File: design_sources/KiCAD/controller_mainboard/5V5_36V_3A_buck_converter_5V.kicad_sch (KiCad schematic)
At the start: 13 parts, among them U5 TPS5430DDA

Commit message: Continued development on the schematic. Pins wired. TODO validate.
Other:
- company: Kestech -> Mete Han Keskin
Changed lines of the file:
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@@
 		(date "2025-03-01")
 		(rev "V1.0")
-		(company "Kestech")
-		(comment 1 "MIT License. Copyright (c) 2025 Kestech Fontys")
+		(company "Mete Han Keskin")
+		(comment 1 "MIT License. Copyright (c) 2025 kestech.net")
 	)
 	(text "Vout is 4.88V specifically"

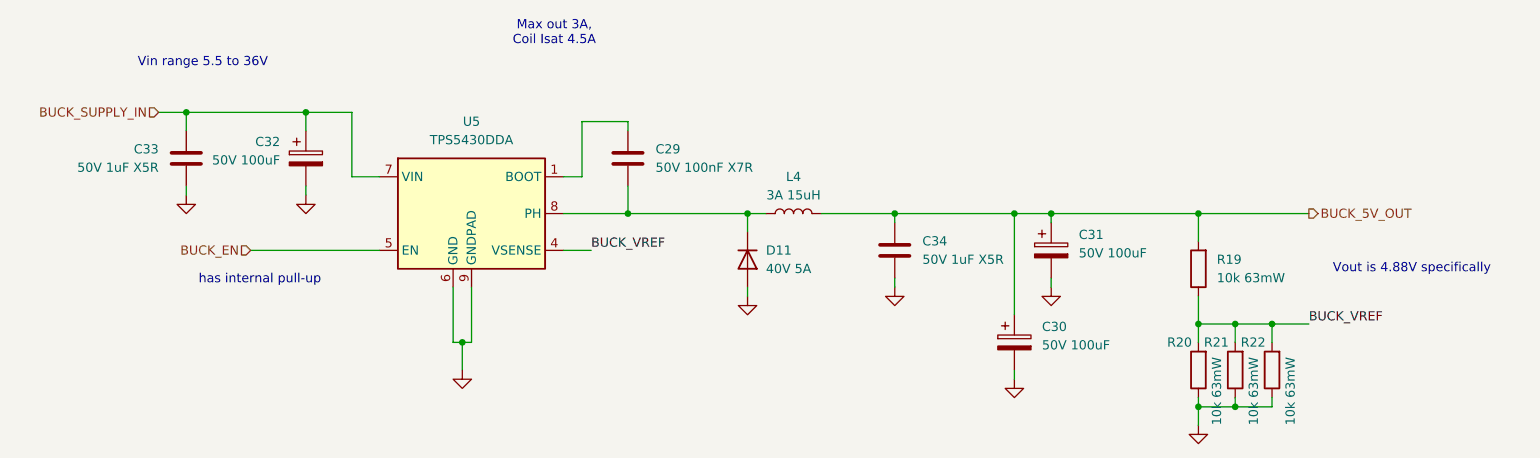
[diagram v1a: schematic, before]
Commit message: Added ESD protection ic, added footprints to all IC and loaded into pcbnew to size up the pcb size.
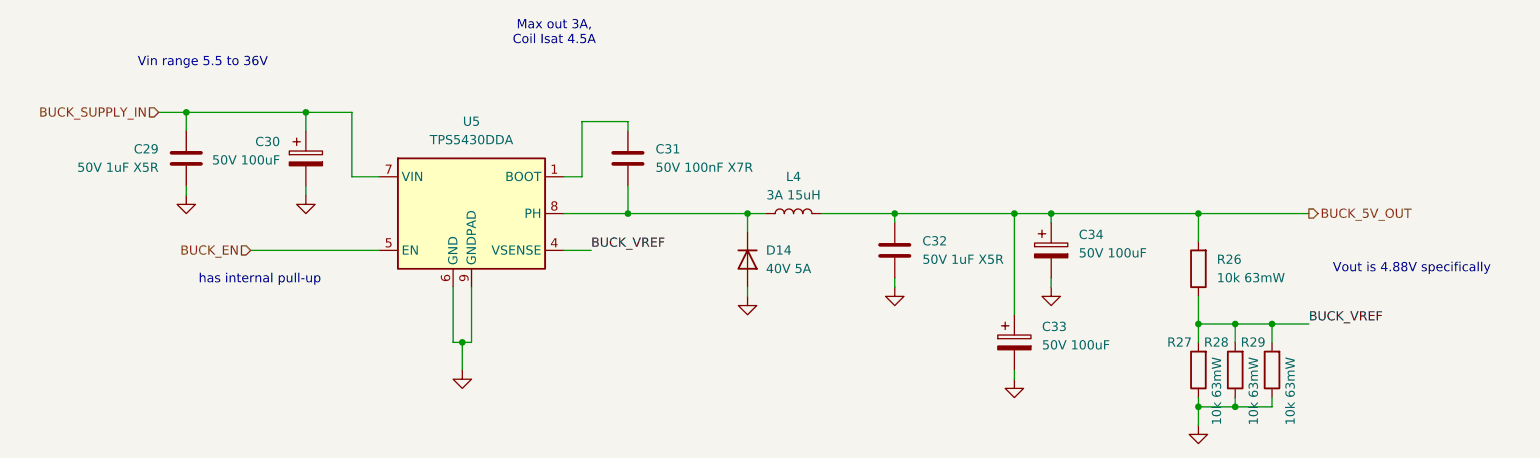
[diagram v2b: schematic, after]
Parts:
- L4: footprint (none) -> Inductor_SMD:L_APV_APH0630
- renumbered C33 to C29, C32 to C30, C29 to C31, C34 to C32, C30 to C33, C31 to C34, D11 to D14, R19 to R26, R20 to R27, R21 to R28, R22 to R29
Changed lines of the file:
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@@
 		(dnp no)
 		(fields_autoplaced yes)
-		(property "Reference" "#PWR031"
+		(property "Reference" "#PWR077"
 			(at 161.29 101.6 0)
 			(effects
@@
 			(project "controller_mainboard"
 				(path "/0fdfffec-3d24-4249-8ba9-dae7a6ccc250/f942a5b5-54c0-4fcc-a043-1f1cc07d1d6d"
-					(reference "#PWR031")
+					(reference "#PWR077")
 					(unit 1)
 				)
@@
 		(dnp no)
 		(fields_autoplaced yes)
-		(property "Reference" "#PWR033"
+		(property "Reference" "#PWR079"
 			(at 182.88 101.6 0)
 			(effects
@@
 			(project "controller_mainboard"
 				(path "/0fdfffec-3d24-4249-8ba9-dae7a6ccc250/f942a5b5-54c0-4fcc-a043-1f1cc07d1d6d"
-					(reference "#PWR033")
+					(reference "#PWR079")
 					(unit 1)
 				)
@@
 		(dnp no)
 		(fields_autoplaced yes)
-		(property "Reference" "C31"
+		(property "Reference" "C34"
 			(at 186.69 88.0109 0)
 			(effects
@@
 			(project "controller_mainboard"
 				(path "/0fdfffec-3d24-4249-8ba9-dae7a6ccc250/f942a5b5-54c0-4fcc-a043-1f1cc07d1d6d"
-					(reference "C31")
+					(reference "C34")
 					(unit 1)
 				)
@@
 		(dnp no)
 		(fields_autoplaced yes)
-		(property "Reference" "#PWR035"
+		(property "Reference" "#PWR076"
 			(at 140.97 102.87 0)
 			(effects
@@
 			(project "controller_mainboard"
 				(path "/0fdfffec-3d24-4249-8ba9-dae7a6ccc250/f942a5b5-54c0-4fcc-a043-1f1cc07d1d6d"
-					(reference "#PWR035")
+					(reference "#PWR076")
 					(unit 1)
 				)
@@
 		(dnp no)
 		(fields_autoplaced yes)
-		(property "Reference" "#PWR030"
+		(property "Reference" "#PWR074"
 			(at 80.01 88.9 0)
 			(effects
@@
 			(project "controller_mainboard"
 				(path "/0fdfffec-3d24-4249-8ba9-dae7a6ccc250/f942a5b5-54c0-4fcc-a043-1f1cc07d1d6d"
-					(reference "#PWR030")
+					(reference "#PWR074")
 					(unit 1)
 				)
@@
 		(dnp no)
 		(fields_autoplaced yes)
-		(property "Reference" "C30"
+		(property "Reference" "C33"
 			(at 181.61 100.7109 0)
 			(effects
@@
 			(project "controller_mainboard"
 				(path "/0fdfffec-3d24-4249-8ba9-dae7a6ccc250/f942a5b5-54c0-4fcc-a043-1f1cc07d1d6d"
-					(reference "C30")
+					(reference "C33")
 					(unit 1)
 				)
@@
 		(on_board yes)
 		(dnp no)
-		(property "Reference" "R21"
+		(property "Reference" "R28"
 			(at 203.962 102.87 0)
 			(effects
@@
 			(project "controller_mainboard"
 				(path "/0fdfffec-3d24-4249-8ba9-dae7a6ccc250/f942a5b5-54c0-4fcc-a043-1f1cc07d1d6d"
-					(reference "R21")
+					(reference "R28")
 					(unit 1)
 				)
@@
 		(dnp no)
 		(fields_autoplaced yes)
-		(property "Reference" "#PWR036"
+		(property "Reference" "#PWR080"
 			(at 203.2 120.65 0)
 			(effects
@@
 			(project "controller_mainboard"
 				(path "/0fdfffec-3d24-4249-8ba9-dae7a6ccc250/f942a5b5-54c0-4fcc-a043-1f1cc07d1d6d"
-					(reference "#PWR036")
+					(reference "#PWR080")
 					(unit 1)
 				)
@@
 		(dnp no)
 		(fields_autoplaced yes)
-		(property "Reference" "C29"
+		(property "Reference" "C31"
 			(at 128.27 76.1999 0)
 			(effects
@@
 			(project "controller_mainboard"
 				(path "/0fdfffec-3d24-4249-8ba9-dae7a6ccc250/f942a5b5-54c0-4fcc-a043-1f1cc07d1d6d"
-					(reference "C29")
+					(reference "C31")
 					(unit 1)
 				)
@@
 		(on_board yes)
 		(dnp no)
-		(property "Reference" "R22"
+		(property "Reference" "R29"
 			(at 209.042 102.87 0)
 			(effects
@@
 			(project "controller_mainboard"
 				(path "/0fdfffec-3d24-4249-8ba9-dae7a6ccc250/f942a5b5-54c0-4fcc-a043-1f1cc07d1d6d"
-					(reference "R22")
+					(reference "R29")
 					(unit 1)
 				)
@@
 		(dnp no)
 		(fields_autoplaced yes)
-		(property "Reference" "R19"
+		(property "Reference" "R26"
 			(at 205.74 91.4399 0)
 			(effects
@@
 			(project "controller_mainboard"
 				(path "/0fdfffec-3d24-4249-8ba9-dae7a6ccc250/f942a5b5-54c0-4fcc-a043-1f1cc07d1d6d"
-					(reference "R19")
+					(reference "R26")
 					(unit 1)
 				)
@@
 			)
 		)
-		(property "Footprint" ""
+		(property "Footprint" "Inductor_SMD:L_APV_APH0630"
 			(at 147.32 85.09 0)
 			(effects
@@
 		(dnp no)
 		(fields_autoplaced yes)
-		(property "Reference" "C33"
+		(property "Reference" "C29"
 			(at 59.69 76.1999 0)
 			(effects
@@
 			(project "controller_mainboard"
 				(path "/0fdfffec-3d24-4249-8ba9-dae7a6ccc250/f942a5b5-54c0-4fcc-a043-1f1cc07d1d6d"
-					(reference "C33")
+					(reference "C29")
 					(unit 1)
 				)
@@
 		(on_board yes)
 		(dnp no)
-		(property "Reference" "C34"
+		(property "Reference" "C32"
 			(at 165.1 88.8999 0)
 			(effects
@@
 			(project "controller_mainboard"
 				(path "/0fdfffec-3d24-4249-8ba9-dae7a6ccc250/f942a5b5-54c0-4fcc-a043-1f1cc07d1d6d"
-					(reference "C34")
+					(reference "C32")
 					(unit 1)
 				)
@@
 		(on_board yes)
 		(dnp no)
-		(property "Reference" "C32"
+		(property "Reference" "C30"
 			(at 76.454 75.184 0)
 			(effects
@@
 			(project "controller_mainboard"
 				(path "/0fdfffec-3d24-4249-8ba9-dae7a6ccc250/f942a5b5-54c0-4fcc-a043-1f1cc07d1d6d"
-					(reference "C32")
+					(reference "C30")
 					(unit 1)
 				)
@@
 		(dnp no)
 		(fields_autoplaced yes)
-		(property "Reference" "#PWR029"
+		(property "Reference" "#PWR075"
 			(at 101.6 113.03 0)
 			(effects
@@
 			(project "controller_mainboard"
 				(path "/0fdfffec-3d24-4249-8ba9-dae7a6ccc250/f942a5b5-54c0-4fcc-a043-1f1cc07d1d6d"
-					(reference "#PWR029")
+					(reference "#PWR075")
 					(unit 1)
 				)
@@
 		(on_board yes)
 		(dnp no)
-		(property "Reference" "D11"
+		(property "Reference" "D14"
 			(at 143.51 90.1699 90)
 			(effects
@@
 			(project "controller_mainboard"
 				(path "/0fdfffec-3d24-4249-8ba9-dae7a6ccc250/f942a5b5-54c0-4fcc-a043-1f1cc07d1d6d"
-					(reference "D11")
+					(reference "D14")
 					(unit 1)
 				)
@@
 		(on_board yes)
 		(dnp no)
-		(property "Reference" "R20"
+		(property "Reference" "R27"
 			(at 198.882 102.87 0)
 			(effects
@@
 			(project "controller_mainboard"
 				(path "/0fdfffec-3d24-4249-8ba9-dae7a6ccc250/f942a5b5-54c0-4fcc-a043-1f1cc07d1d6d"
-					(reference "R20")
+					(reference "R27")
 					(unit 1)
 				)
@@
 		(dnp no)
 		(fields_autoplaced yes)
-		(property "Reference" "#PWR032"
+		(property "Reference" "#PWR078"
 			(at 177.8 114.3 0)
 			(effects
@@
 			(project "controller_mainboard"
 				(path "/0fdfffec-3d24-4249-8ba9-dae7a6ccc250/f942a5b5-54c0-4fcc-a043-1f1cc07d1d6d"
-					(reference "#PWR032")
+					(reference "#PWR078")
 					(unit 1)
 				)
@@
 		(dnp no)
 		(fields_autoplaced yes)
-		(property "Reference" "#PWR034"
+		(property "Reference" "#PWR073"
 			(at 63.5 88.9 0)
 			(effects
@@
 			(project "controller_mainboard"
 				(path "/0fdfffec-3d24-4249-8ba9-dae7a6ccc250/f942a5b5-54c0-4fcc-a043-1f1cc07d1d6d"
-					(reference "#PWR034")
-					(unit 1)
-				)
+					(reference "#PWR073")
+					(unit 1)
+				)

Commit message: Changed JLCPCB field to LCSC
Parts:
- C29, C32: JLCPCB C15849 -> (none); LCSC (none) -> C15849
- C30, C33, C34: JLCPCB C5246561 -> (none); LCSC (none) -> C5246561
- C31: JLCPCB C14663 -> (none); LCSC (none) -> C14663
- D14: JLCPCB C22452 -> (none); LCSC (none) -> C22452
- L4: JLCPCB C177243 -> (none); LCSC (none) -> C177243
- R26, R27, R28, R29: JLCPCB C25744 -> (none); LCSC (none) -> C25744
- U5: JLCPCB C9864 -> (none); LCSC (none) -> C9864
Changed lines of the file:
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@@
 			)
 		)
-		(property "JLCPCB" "C5246561"
+		(property "LCSC" "C5246561"
 			(at 182.88 90.17 0)
 			(effects
@@
 			)
 		)
-		(property "JLCPCB" "C5246561"
+		(property "LCSC" "C5246561"
 			(at 177.8 102.87 0)
 			(effects
@@
 			)
 		)
-		(property "JLCPCB" "C25744"
+		(property "LCSC" "C25744"
 			(at 208.28 106.68 0)
 			(effects
@@
 			)
 		)
-		(property "JLCPCB" "C14663"
+		(property "LCSC" "C14663"
 			(at 124.46 77.47 0)
 			(effects
@@
 			)
 		)
-		(property "JLCPCB" "C25744"
+		(property "LCSC" "C25744"
 			(at 213.36 106.68 0)
 			(effects
@@
 			)
 		)
-		(property "JLCPCB" "C9864"
+		(property "LCSC" "C9864"
 			(at 102.87 85.09 0)
 			(effects
@@
 			)
 		)
-		(property "JLCPCB" "C25744"
+		(property "LCSC" "C25744"
 			(at 203.2 92.71 0)
 			(effects
@@
 			)
 		)
-		(property "JLCPCB" "C177243"
+		(property "LCSC" "C177243"
 			(at 147.32 85.09 90)
 			(effects
@@
 			)
 		)
-		(property "JLCPCB" "C15849"
+		(property "LCSC" "C15849"
 			(at 63.5 77.47 0)
 			(effects
@@
 			)
 		)
-		(property "JLCPCB" "C15849"
+		(property "LCSC" "C15849"
 			(at 161.29 90.17 0)
 			(effects
@@
 			)
 		)
-		(property "JLCPCB" "C5246561"
+		(property "LCSC" "C5246561"
 			(at 80.01 77.47 0)
 			(effects
@@
 			)
 		)
-		(property "JLCPCB" "C22452"
+		(property "LCSC" "C22452"
 			(at 140.97 91.44 90)
 			(effects
@@
 			)
 		)
-		(property "JLCPCB" "C25744"
+		(property "LCSC" "C25744"
 			(at 203.2 106.68 0)
 			(effects
